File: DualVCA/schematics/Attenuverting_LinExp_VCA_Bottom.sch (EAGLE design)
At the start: 203 parts, among them IC1 TL074D, IC10 TL074D, IC12 QUAD_OPAMPD, IC13 LM4041C12DBZ, IC14 QUAD_OPAMPD, IC2 SSM2164S, IC3 TL074D, IC4 TL072D, IC5 TL074D, IC6 SSM2164S, IC7 TL074D, IC8 TL074D, IC9 TL074D, Q10 BSS123, Q9 BSS84

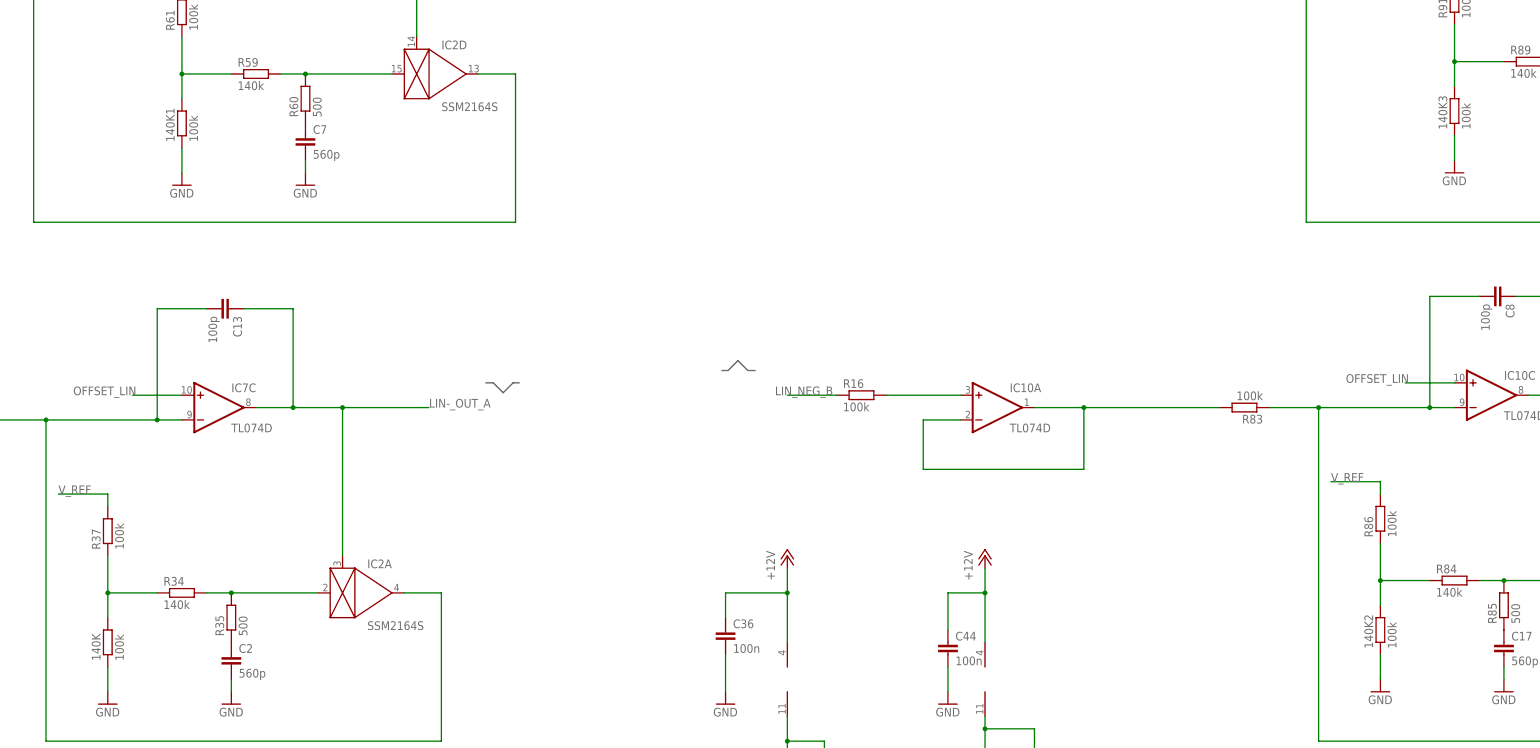
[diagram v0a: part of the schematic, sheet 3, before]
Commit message: Labelling Completed Top and Bottom
- Front Panel Layout Changed

- Labelling Completed
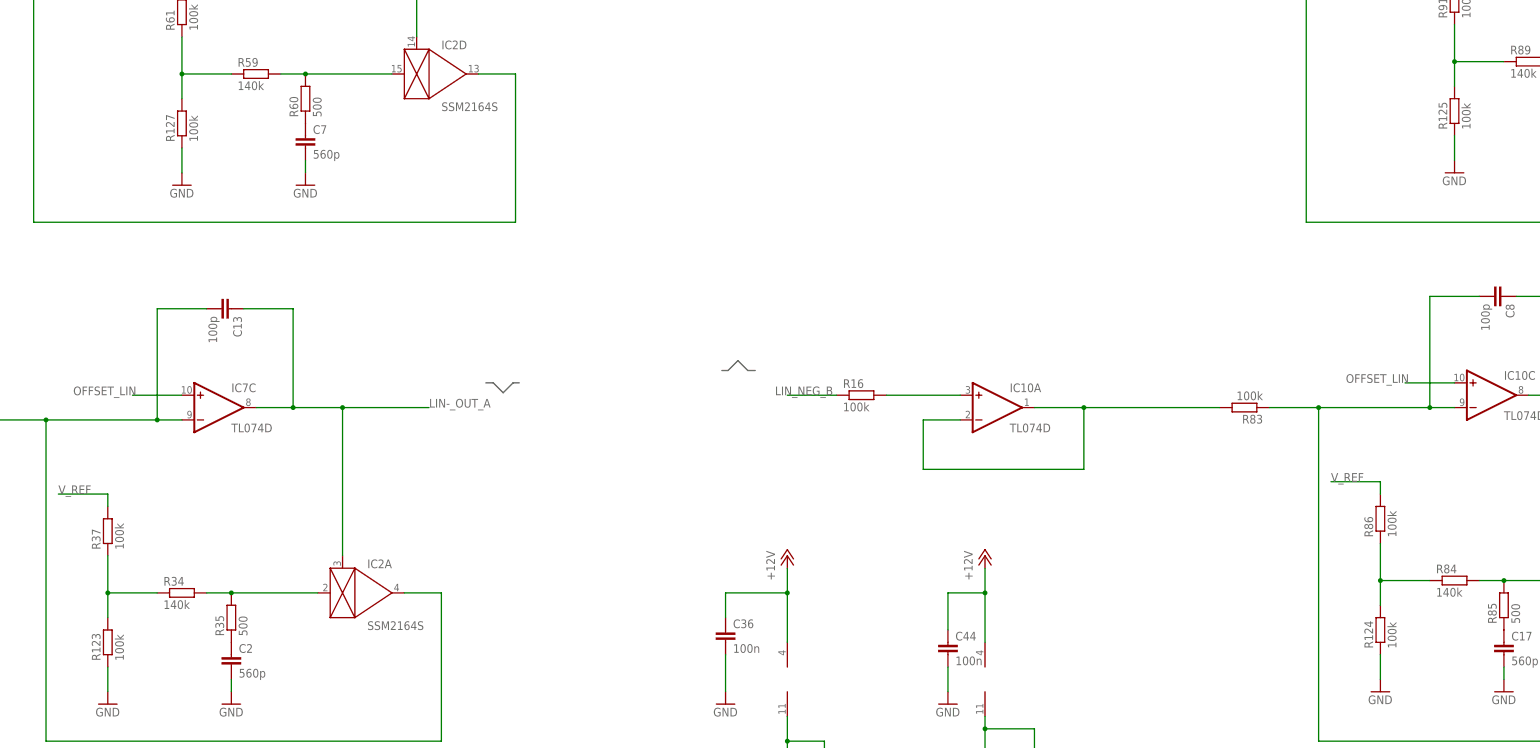
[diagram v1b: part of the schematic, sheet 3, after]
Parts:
- renumbered 140K to R123, 140K1 to R127, 140K2 to R124, 140K3 to R125, 1K to R126, 1K1 to R115
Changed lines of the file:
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@@
 <?xml version="1.0" encoding="utf-8"?>
 <!DOCTYPE eagle SYSTEM "eagle.dtd">
-<eagle version="7.7.0">
+<eagle version="8.3.2">
 <drawing>
 <settings>
 <setting alwaysvectorfont="no"/>
+<setting keepoldvectorfont="yes"/>
 <setting verticaltext="up"/>
 </settings>
@@
 <attribute name="OC_FARNELL" value="unknown"/>
 </part>
-<part name="1K" library="Rebel" deviceset="R-EU_" device="0603" value="1k">
+<part name="R126" library="Rebel" deviceset="R-EU_" device="0603" value="1k">
 <attribute name="MF" value="MULTICOMP"/>
 <attribute name="MPN" value="MC0063W06031160K"/>
@@
 <attribute name="OC_FARNELL" value="unknown"/>
 </part>
-<part name="140K" library="Rebel" deviceset="R-EU_" device="0603" value="100k">
+<part name="R123" library="Rebel" deviceset="R-EU_" device="0603" value="100k">
 <attribute name="MF" value=""/>
 <attribute name="MPN" value=""/>
@@
 <attribute name="OC_FARNELL" value="unknown"/>
 </part>
-<part name="140K1" library="Rebel" deviceset="R-EU_" device="0603" value="100k">
+<part name="R127" library="Rebel" deviceset="R-EU_" device="0603" value="100k">
 <attribute name="MF" value=""/>
 <attribute name="MPN" value=""/>
@@
 <attribute name="OC_FARNELL" value="unknown"/>
 </part>
-<part name="1K1" library="Rebel" deviceset="R-EU_" device="0603" value="1k">
+<part name="R115" library="Rebel" deviceset="R-EU_" device="0603" value="1k">
 <attribute name="MF" value="MULTICOMP"/>
 <attribute name="MPN" value="MC0063W06031160K"/>
@@
 <attribute name="OC_FARNELL" value="unknown"/>
 </part>
-<part name="140K2" library="Rebel" deviceset="R-EU_" device="0603" value="100k">
+<part name="R124" library="Rebel" deviceset="R-EU_" device="0603" value="100k">
 <attribute name="MF" value=""/>
 <attribute name="MPN" value=""/>
@@
 <attribute name="OC_FARNELL" value="unknown"/>
 </part>
-<part name="140K3" library="Rebel" deviceset="R-EU_" device="0603" value="100k">
+<part name="R125" library="Rebel" deviceset="R-EU_" device="0603" value="100k">
 <attribute name="MF" value=""/>
 <attribute name="MPN" value=""/>
@@
 <attribute name="MPN" x="28.956" y="-259.08" size="1.778" layer="96" rot="R90" display="off"/>
 </instance>
-<instance part="1K" gate="G$1" x="66.548" y="-271.78">
+<instance part="R126" gate="G$1" x="66.548" y="-271.78">
 <attribute name="OC_FARNELL" x="66.548" y="-271.78" size="1.778" layer="96" rot="R90" display="off"/>
 <attribute name="MF" x="66.548" y="-271.78" size="1.778" layer="96" rot="R90" display="off"/>
@@
 <attribute name="MPN" x="473.964" y="-264.16" size="1.778" layer="96" rot="R90" display="off"/>
 </instance>
-<instance part="1K1" gate="G$1" x="511.048" y="-276.86">
+<instance part="R115" gate="G$1" x="511.048" y="-276.86">
 <attribute name="OC_FARNELL" x="511.048" y="-276.86" size="1.778" layer="96" rot="R90" display="off"/>
 <attribute name="MF" x="511.048" y="-276.86" size="1.778" layer="96" rot="R90" display="off"/>
@@
 <net name="OUT_A" class="0">
 <segment>
-<pinref part="1K" gate="G$1" pin="2"/>
+<pinref part="R126" gate="G$1" pin="2"/>
 <wire x1="71.628" y1="-271.78" x2="78.232" y2="-271.78" width="0.1524" layer="91"/>
 <label x="78.486" y="-271.78" size="1.778" layer="95"/>
@@
 <wire x1="51.054" y1="-259.08" x2="34.036" y2="-259.08" width="0.1524" layer="91"/>
 <wire x1="51.054" y1="-271.78" x2="61.468" y2="-271.78" width="0.1524" layer="91"/>
-<pinref part="1K" gate="G$1" pin="1"/>
+<pinref part="R126" gate="G$1" pin="1"/>
 <junction x="51.054" y="-271.78"/>
 </segment>
@@
 <wire x1="495.554" y1="-264.16" x2="479.044" y2="-264.16" width="0.1524" layer="91"/>
 <wire x1="495.554" y1="-276.86" x2="505.968" y2="-276.86" width="0.1524" layer="91"/>
-<pinref part="1K1" gate="G$1" pin="1"/>
+<pinref part="R115" gate="G$1" pin="1"/>
 <junction x="495.554" y="-276.86"/>
 </segment>
@@
 <net name="OUT_B" class="0">
 <segment>
-<pinref part="1K1" gate="G$1" pin="2"/>
+<pinref part="R115" gate="G$1" pin="2"/>
 <wire x1="516.128" y1="-276.86" x2="522.732" y2="-276.86" width="0.1524" layer="91"/>
 <label x="522.986" y="-276.86" size="1.778" layer="95"/>
@@
 <attribute name="MPN" x="142.24" y="93.98" size="1.778" layer="96" rot="R90" display="off"/>
 </instance>
-<instance part="140K1" gate="G$1" x="142.24" y="71.12" rot="R90">
+<instance part="R127" gate="G$1" x="142.24" y="71.12" rot="R90">
 <attribute name="OC_FARNELL" x="142.24" y="71.12" size="1.778" layer="96" rot="R90" display="off"/>
 <attribute name="MF" x="142.24" y="71.12" size="1.778" layer="96" rot="R90" display="off"/>
@@
 <attribute name="MPN" x="127" y="-12.7" size="1.778" layer="96" rot="R90" display="off"/>
 </instance>
-<instance part="140K" gate="G$1" x="127" y="-35.56" rot="R90">
+<instance part="R123" gate="G$1" x="127" y="-35.56" rot="R90">
 <attribute name="OC_FARNELL" x="127" y="-35.56" size="1.778" layer="96" rot="R90" display="off"/>
 <attribute name="MF" x="127" y="-35.56" size="1.778" layer="96" rot="R90" display="off"/>
@@
 <attribute name="MPN" x="403.86" y="96.52" size="1.778" layer="96" rot="R90" display="off"/>
 </instance>
-<instance part="140K3" gate="G$1" x="403.86" y="73.66" rot="R90">
+<instance part="R125" gate="G$1" x="403.86" y="73.66" rot="R90">
 <attribute name="OC_FARNELL" x="403.86" y="73.66" size="1.778" layer="96" rot="R90" display="off"/>
 <attribute name="MF" x="403.86" y="73.66" size="1.778" layer="96" rot="R90" display="off"/>
@@
 <attribute name="MPN" x="388.62" y="-10.16" size="1.778" layer="96" rot="R90" display="off"/>
 </instance>
-<instance part="140K2" gate="G$1" x="388.62" y="-33.02" rot="R90">
+<instance part="R124" gate="G$1" x="388.62" y="-33.02" rot="R90">
 <attribute name="OC_FARNELL" x="388.62" y="-33.02" size="1.778" layer="96" rot="R90" display="off"/>
 <attribute name="MF" x="388.62" y="-33.02" size="1.778" layer="96" rot="R90" display="off"/>
@@
 <segment>
 <pinref part="GND22" gate="1" pin="GND"/>
-<pinref part="140K1" gate="G$1" pin="1"/>
+<pinref part="R127" gate="G$1" pin="1"/>
 <wire x1="142.24" y1="60.96" x2="142.24" y2="66.04" width="0.1524" layer="91"/>
 </segment>
@@
 <segment>
 <pinref part="GND14" gate="1" pin="GND"/>
-<pinref part="140K" gate="G$1" pin="1"/>
+<pinref part="R123" gate="G$1" pin="1"/>
 <wire x1="127" y1="-45.72" x2="127" y2="-40.64" width="0.1524" layer="91"/>
 </segment>
@@
 <segment>
 <pinref part="GND37" gate="1" pin="GND"/>
-<pinref part="140K3" gate="G$1" pin="1"/>
+<pinref part="R125" gate="G$1" pin="1"/>
 <wire x1="403.86" y1="63.5" x2="403.86" y2="68.58" width="0.1524" layer="91"/>
 </segment>
@@
 <segment>
 <pinref part="GND35" gate="1" pin="GND"/>
-<pinref part="140K2" gate="G$1" pin="1"/>
+<pinref part="R124" gate="G$1" pin="1"/>
 <wire x1="388.62" y1="-43.18" x2="388.62" y2="-38.1" width="0.1524" layer="91"/>
 </segment>
@@
 <pinref part="R61" gate="G$1" pin="1"/>
 <wire x1="142.24" y1="81.28" x2="142.24" y2="88.9" width="0.1524" layer="91"/>
-<pinref part="140K1" gate="G$1" pin="2"/>
+<pinref part="R127" gate="G$1" pin="2"/>
 <wire x1="142.24" y1="76.2" x2="142.24" y2="81.28" width="0.1524" layer="91"/>
 <junction x="142.24" y="81.28"/>
@@
 <pinref part="R37" gate="G$1" pin="1"/>
 <wire x1="127" y1="-25.4" x2="127" y2="-17.78" width="0.1524" layer="91"/>
-<pinref part="140K" gate="G$1" pin="2"/>
+<pinref part="R123" gate="G$1" pin="2"/>
 <wire x1="127" y1="-30.48" x2="127" y2="-25.4" width="0.1524" layer="91"/>
 <junction x="127" y="-25.4"/>
@@
 <pinref part="R91" gate="G$1" pin="1"/>
 <wire x1="403.86" y1="83.82" x2="403.86" y2="91.44" width="0.1524" layer="91"/>
-<pinref part="140K3" gate="G$1" pin="2"/>
+<pinref part="R125" gate="G$1" pin="2"/>
 <wire x1="403.86" y1="78.74" x2="403.86" y2="83.82" width="0.1524" layer="91"/>
 <junction x="403.86" y="83.82"/>
@@
 <pinref part="R86" gate="G$1" pin="1"/>
 <wire x1="388.62" y1="-22.86" x2="388.62" y2="-15.24" width="0.1524" layer="91"/>
-<pinref part="140K2" gate="G$1" pin="2"/>
+<pinref part="R124" gate="G$1" pin="2"/>
 <wire x1="388.62" y1="-27.94" x2="388.62" y2="-22.86" width="0.1524" layer="91"/>
 <junction x="388.62" y="-22.86"/>
